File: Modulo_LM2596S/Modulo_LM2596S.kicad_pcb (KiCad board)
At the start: 2 copper layers, 5 parts, among them U101 LM2596S-ADJ

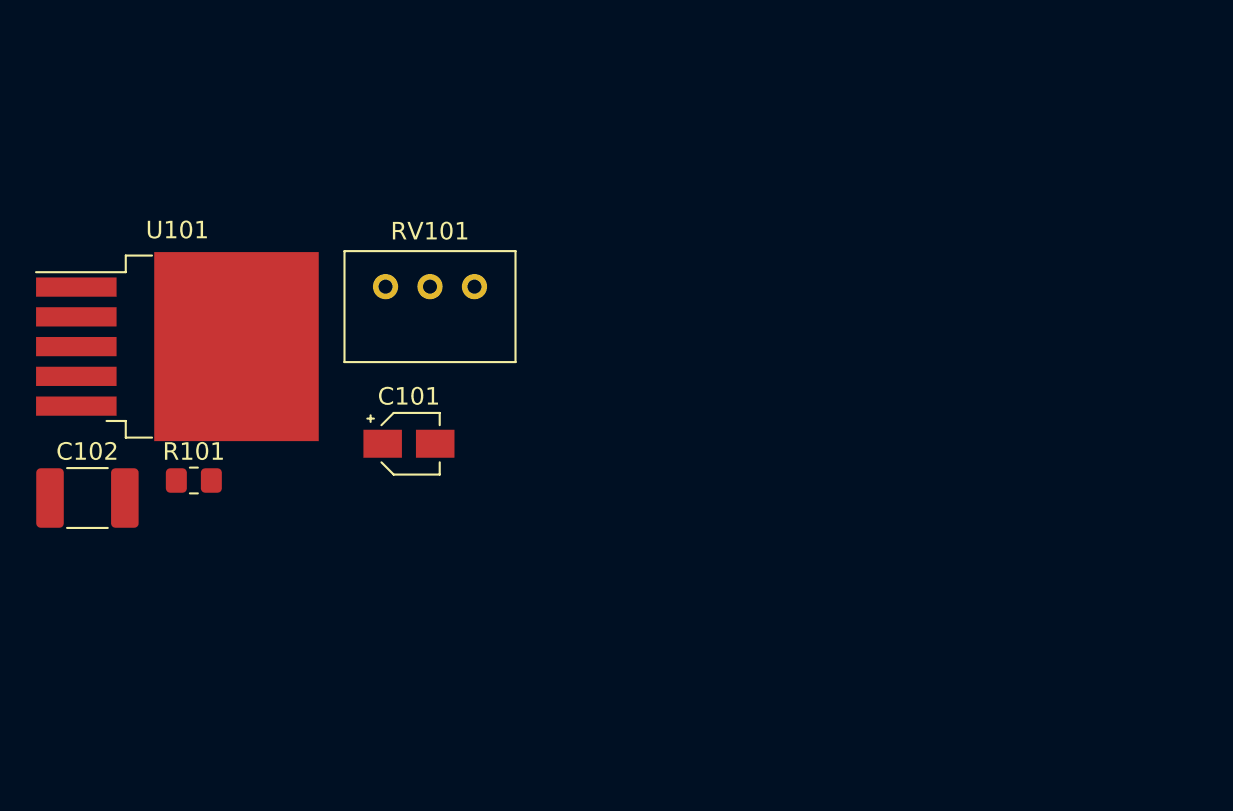
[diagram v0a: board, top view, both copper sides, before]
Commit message: LM2596S: creazione della scheda fisica
Selezione dei componenti e creazione del PCB.
TODO: Da mettere a posto le tracce @GiovanniRaseraF
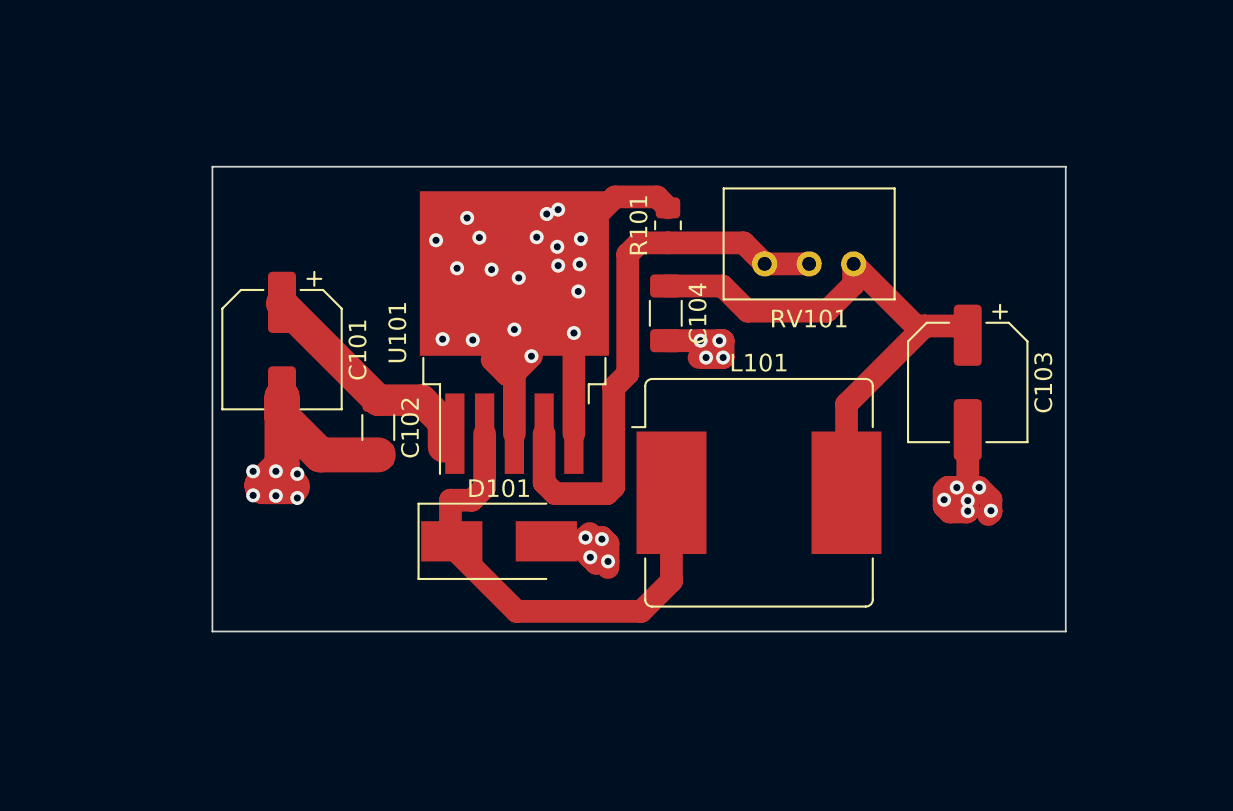
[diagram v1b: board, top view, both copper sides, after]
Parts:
- added C103: 220uF, Capacitor_SMD:CP_Elec_6.3x3.9, F.Cu at (195.0, 80.8)
- added C104: 1uF, Capacitor_SMD:C_1206_3216Metric_Pad1.33x1.80mm_HandSolder, F.Cu at (177.8, 76.8)
- added D101: SS34, Diode_SMD:D_SMB_Handsoldering, F.Cu at (168.2, 89.9)
- added L101: 47uH, Inductor_SMD:L_Bourns_SRR1208_12.7x12.7mm, F.Cu at (183.1, 87.1)
- C101: footprint Capacitor_SMD:CP_Elec_3x5.3 -> Capacitor_SMD:CP_Elec_6.3x3.9
- C102: footprint Capacitor_SMD:C_1812_4532Metric_Pad1.57x3.40mm_HandSolder -> Capacitor_SMD:C_1206_3216Metric_Pad1.33x1.80mm_HandSolder
- moved R101 30.8 mm to (177.9, 71.8), turned to 90 degrees
- moved U101 19.3 mm to (169.1, 78.0), turned to 90 degrees
- moved C102 17.1 mm to (161.3, 83.4), turned to -90 degrees
- moved RV101 16.6 mm to (183.4, 74.0), turned to 180 degrees
- moved C101 9.03 mm to (155.8, 78.9), turned to -90 degrees
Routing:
- net OUT-: track 0.00 -> 55.4 mm, vias 0 -> 33
- net OUT+: track 0.00 -> 32.7 mm
- net Net-(R101-Pad1): track 0.00 -> 32.0 mm
- net Net-(D101-Pad1): track 0.00 -> 27.9 mm
- net Vin-: track 0.00 -> 14.8 mm, vias 0 -> 6
- net Vin+: track 0.00 -> 13.5 mm
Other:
- board outline added: 48.8 x 26.6 mm

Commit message: LM2596: Finito di tirare le tracce
Tirato le tracce e il piano di GND
Inserito io MountPad ed i punti di solder dei cavi di input e output
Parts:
- added H101: MountingHole_Pad, MountingHole:MountingHole_2.2mm_M2_Pad_Via, F.Cu at (154.6, 71.2)
- added H102: MountingHole_Pad, MountingHole:MountingHole_2.2mm_M2_Pad_Via, F.Cu at (198.0, 71.1)
- added H103: MountingHole_Pad, MountingHole:MountingHole_2.2mm_M2_Pad_Via, F.Cu at (154.6, 92.4)
- added H104: MountingHole_Pad, MountingHole:MountingHole_2.2mm_M2_Pad_Via, F.Cu at (197.9, 92.3)
- added J101: Conn_01x01_Female, Connector_Wire:SolderWirePad_1x01_SMD_1x2mm, F.Cu at (153.6, 76.2)
- added J102: Conn_01x01_Female, Connector_Wire:SolderWirePad_1x01_SMD_1x2mm, F.Cu at (198.7, 87.2)
- added J103: Conn_01x01_Female, Connector_Wire:SolderWirePad_1x01_SMD_1x2mm, F.Cu at (198.7, 75.5)
- added J104: Conn_01x01_Female, Connector_Wire:SolderWirePad_1x01_SMD_1x2mm, F.Cu at (153.7, 86.8)
- moved C101 3.58 mm to (158.9, 77.0)
- moved C103 1.70 mm to (194.6, 82.5)
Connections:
- C101 pad 2: Vin- -> OUT-
- C102 pad 2: Vin- -> OUT-
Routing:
- net OUT-: track 55.4 -> 87.2 mm, vias 33 -> 47
- net Vin-: track 14.8 -> 0.00 mm, vias 6 -> 0
- net OUT+: track 32.7 -> 34.1 mm
- net Vin+: track 13.5 -> 14.5 mm
- added copper zone on B.Cu, net OUT-
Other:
- board size 48.8 x 26.6 mm -> 48.8 x 26.5 mm

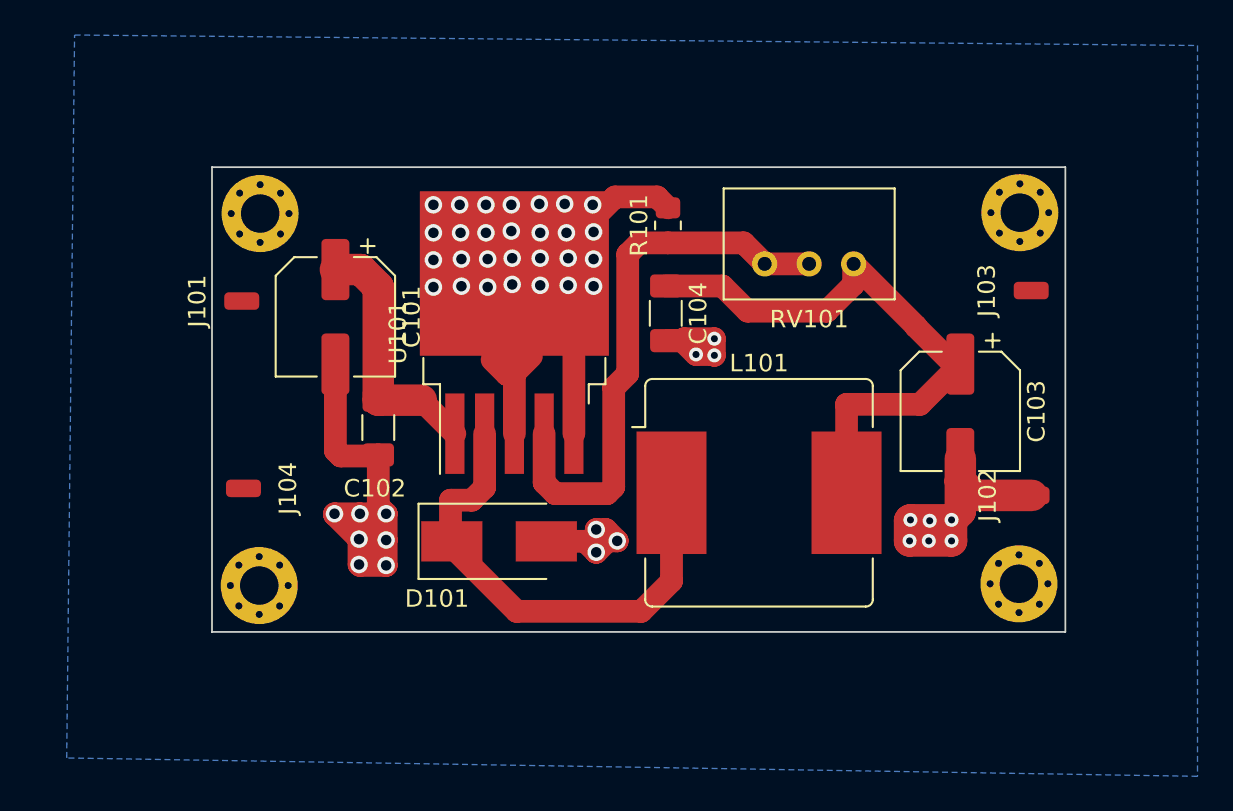
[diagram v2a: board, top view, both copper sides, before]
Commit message: LM2596S: Creazione del layout e inserimento dei solderpoints
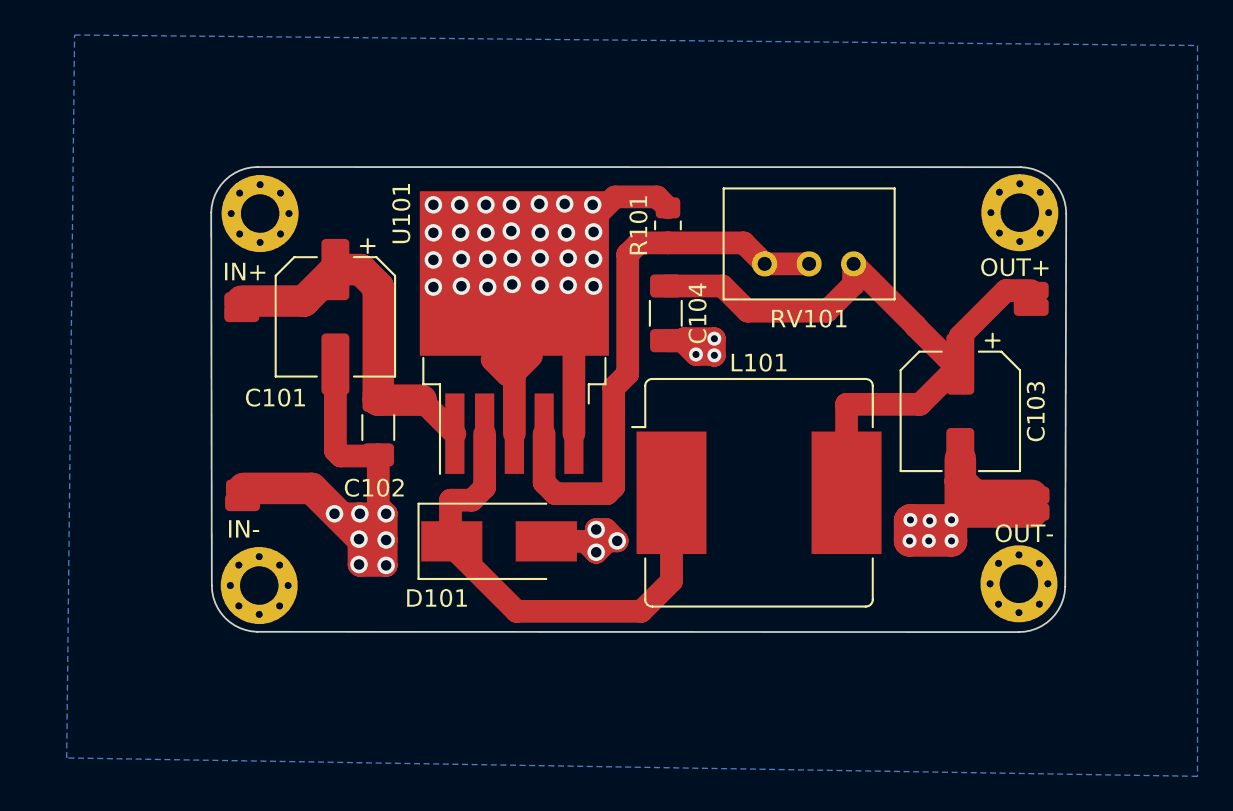
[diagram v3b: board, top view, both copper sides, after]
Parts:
- added J105: Conn_01x01_Female, Connector_Wire:SolderWirePad_1x01_SMD_1x2mm, F.Cu at (153.6, 76.8)
- added J106: Conn_01x01_Female, Connector_Wire:SolderWirePad_1x01_SMD_1x2mm, F.Cu at (198.7, 88.2)
- added J107: Conn_01x01_Female, Connector_Wire:SolderWirePad_1x01_SMD_1x2mm, F.Cu at (198.7, 76.5)
- added J108: Conn_01x01_Female, Connector_Wire:SolderWirePad_1x01_SMD_1x2mm, F.Cu at (153.6, 87.7)
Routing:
- net OUT-: track 87.2 -> 99.7 mm
- net OUT+: track 34.1 -> 40.8 mm
- net Vin+: track 14.5 -> 20.6 mm
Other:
- board size 48.8 x 26.5 mm -> 48.8 x 26.6 mm
- board text added: "Authors: - Cristofoli Nicola - Schematics - Rasera Giovanni - PCB layout https://github.com/GiovanniRaseraF/Vespin2Hardware"
- board text added: "IN+"
- board text added: "IN-"
- board text added: "OUT+"
- board text added: "OUT-"
